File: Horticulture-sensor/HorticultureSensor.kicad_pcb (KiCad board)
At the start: 2 copper layers, 46.9 x 34.8 mm, 15 parts, among them J1 Conn_01x04, J2 Conn_02x05_Odd_Even, J3 Conn_01x03, J4 Conn_01x04, J5 Conn_01x03, J6 Conn_01x04, U1 STM32F030F4Px

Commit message: Resolves #2
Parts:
- moved C1 11.4 mm to (151.4, 129.3), turned to 90 degrees
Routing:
- net i2c-addr_0: track 0.00 -> 11.2 mm
- net i2c-addr_3: track 0.00 -> 9.22 mm
- net +3V3: track 10.3 -> 18.8 mm
- net i2c-addr_2: track 0.00 -> 8.09 mm
- net i2c-addr_1: track 0.00 -> 5.13 mm
- net GND: track 29.9 -> 32.6 mm

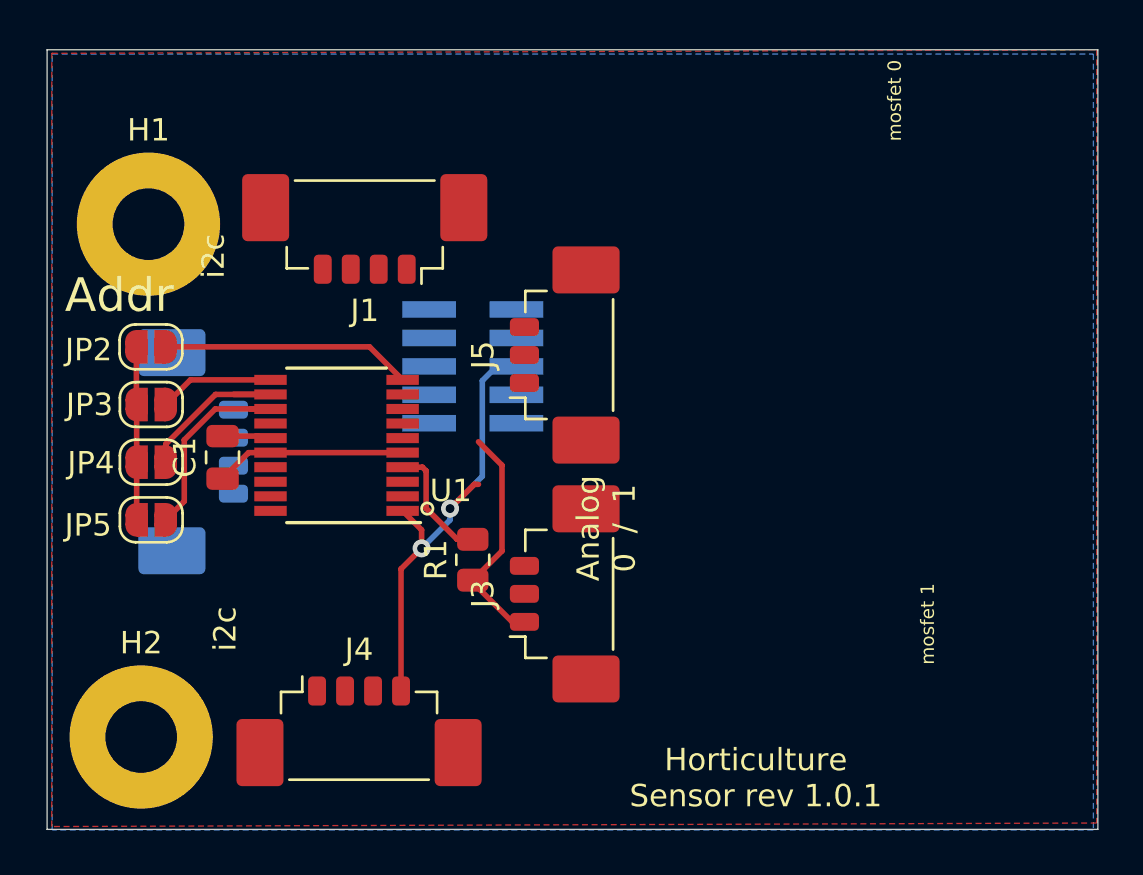
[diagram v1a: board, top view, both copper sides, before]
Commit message: Completed routing
Soilsensor rev 1.0
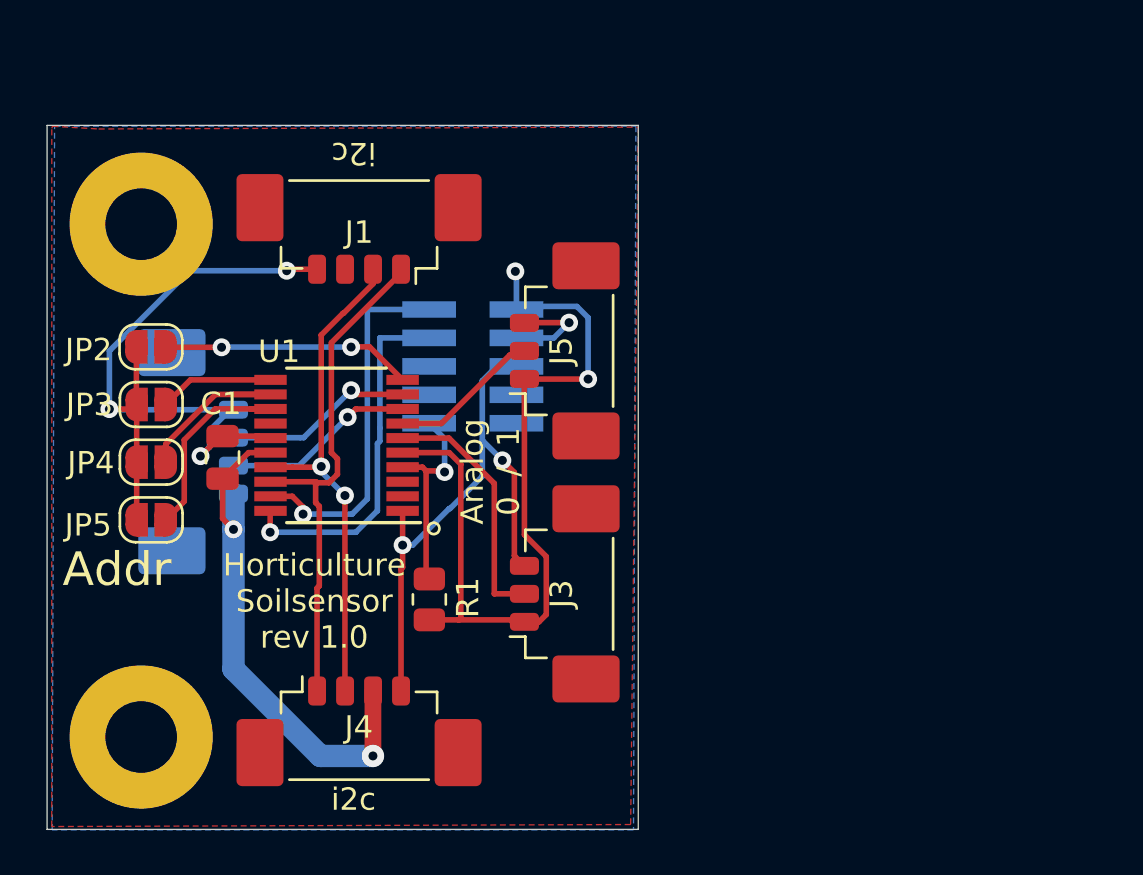
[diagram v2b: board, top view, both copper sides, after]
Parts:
- C1: value C_Small -> 100nF
- R1: value R_Small -> 10k2
- moved R1 2.63 mm to (160.6, 135.6)
- moved H1 0.32 mm to (147.8, 118.9)
- moved J1 0.25 mm to (157.5, 119.6)
- moved J5 0.18 mm to (166.1, 124.5)
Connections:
- J1 pad 3: VCC -> +3V3
- J4 pad 3: VCC -> +3V3
- J6 pad 1: VCC -> +3V3
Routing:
- net +3V3: track 18.8 -> 61.1 mm, vias 0 -> 4
- net GND: track 32.6 -> 66.0 mm, vias 2 -> 6
- net I2c-SDA: track 0.00 -> 23.2 mm
- net I2c-SCL: track 0.00 -> 22.5 mm, vias 0 -> 2
- net SWD-SWIO: track 0.00 -> 16.3 mm, vias 0 -> 1
- net SWD-SWCLK: track 0.00 -> 16.1 mm, vias 0 -> 1
- net AnalogSignal0: track 0.00 -> 11.2 mm
- net UART-tx: track 0.00 -> 8.60 mm, vias 0 -> 1
- net UART-rx: track 0.00 -> 8.51 mm, vias 0 -> 1
- net AnalogSignal1: track 0.00 -> 6.71 mm
- net nRESET: track 5.45 -> 9.32 mm, vias 0 -> 1
- net i2c-addr_0: vias 0 -> 2
- added copper zone on F.Cu, net +3V3
- added copper zone on B.Cu, net GND
- removed copper zone on B.Cu, net +3V3
- removed copper zone on F.Cu, net GND
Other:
- board size 46.9 x 34.8 mm -> 26.4 x 31.4 mm
- board text added: "Horticulture Soilsensor rev 1.0"
- board text removed: "Horticulture Sensor rev 1.0.1"
- board text removed: "mosfet 0"
- board text removed: "mosfet 1"
